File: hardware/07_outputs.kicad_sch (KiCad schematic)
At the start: 13 parts, among them J701 G-Switch GT-3321667P-01, J702 HRO PJ-332A-6A, J703 1 × 6

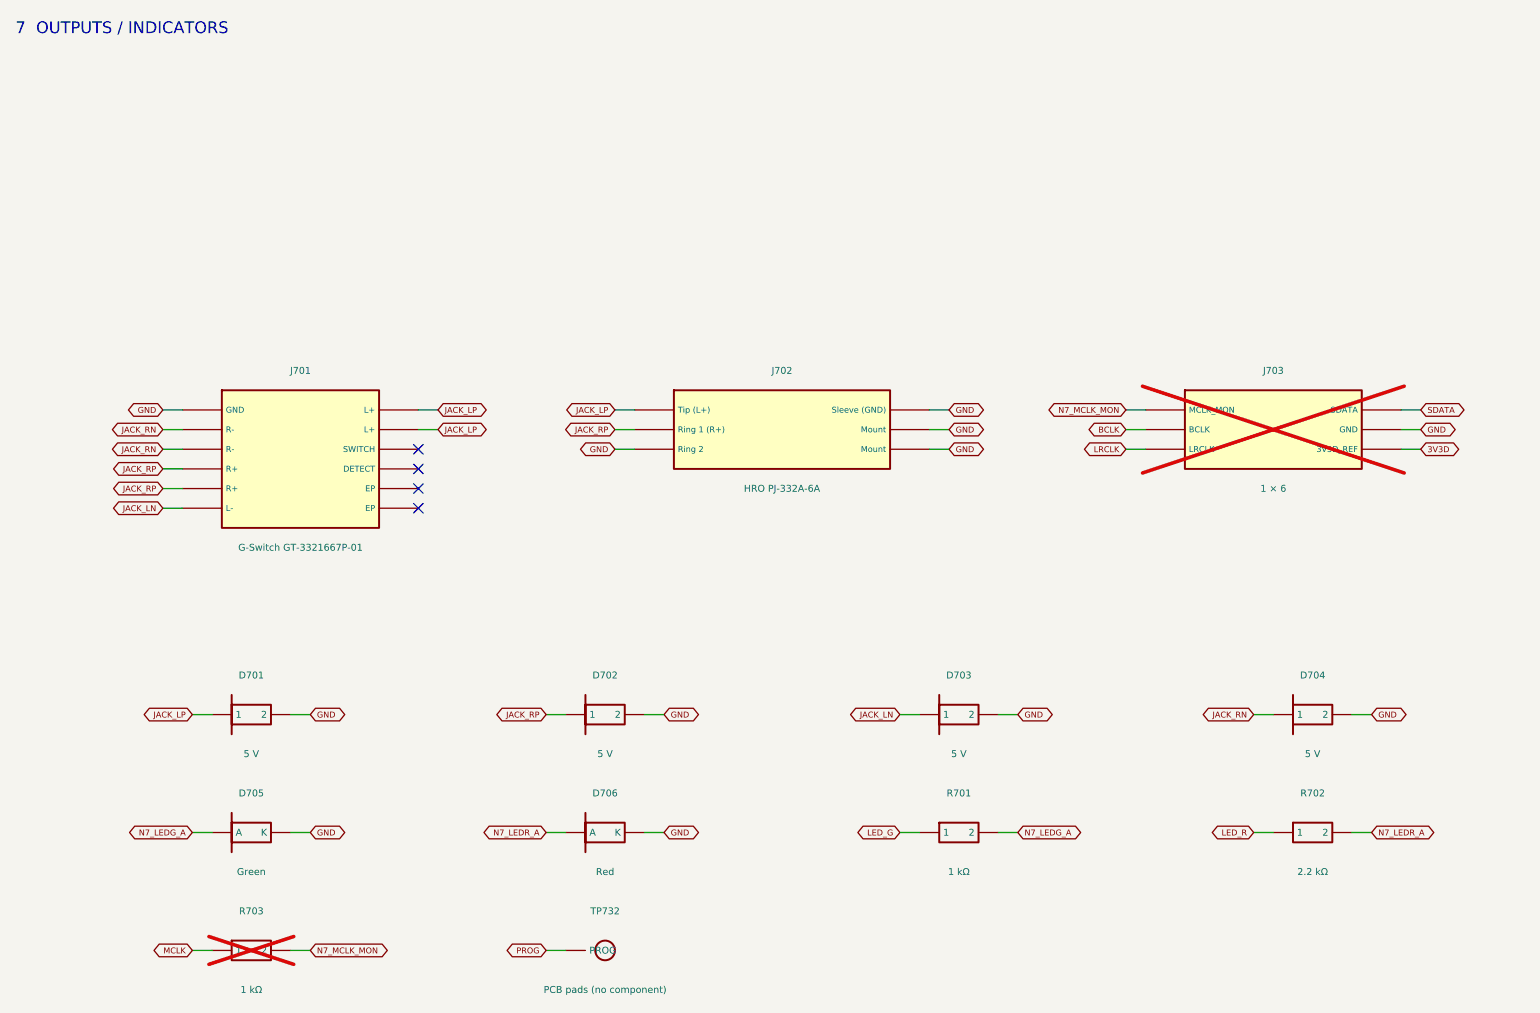
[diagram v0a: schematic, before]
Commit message: Recapture DAC-HPA schematic for design set v1.1
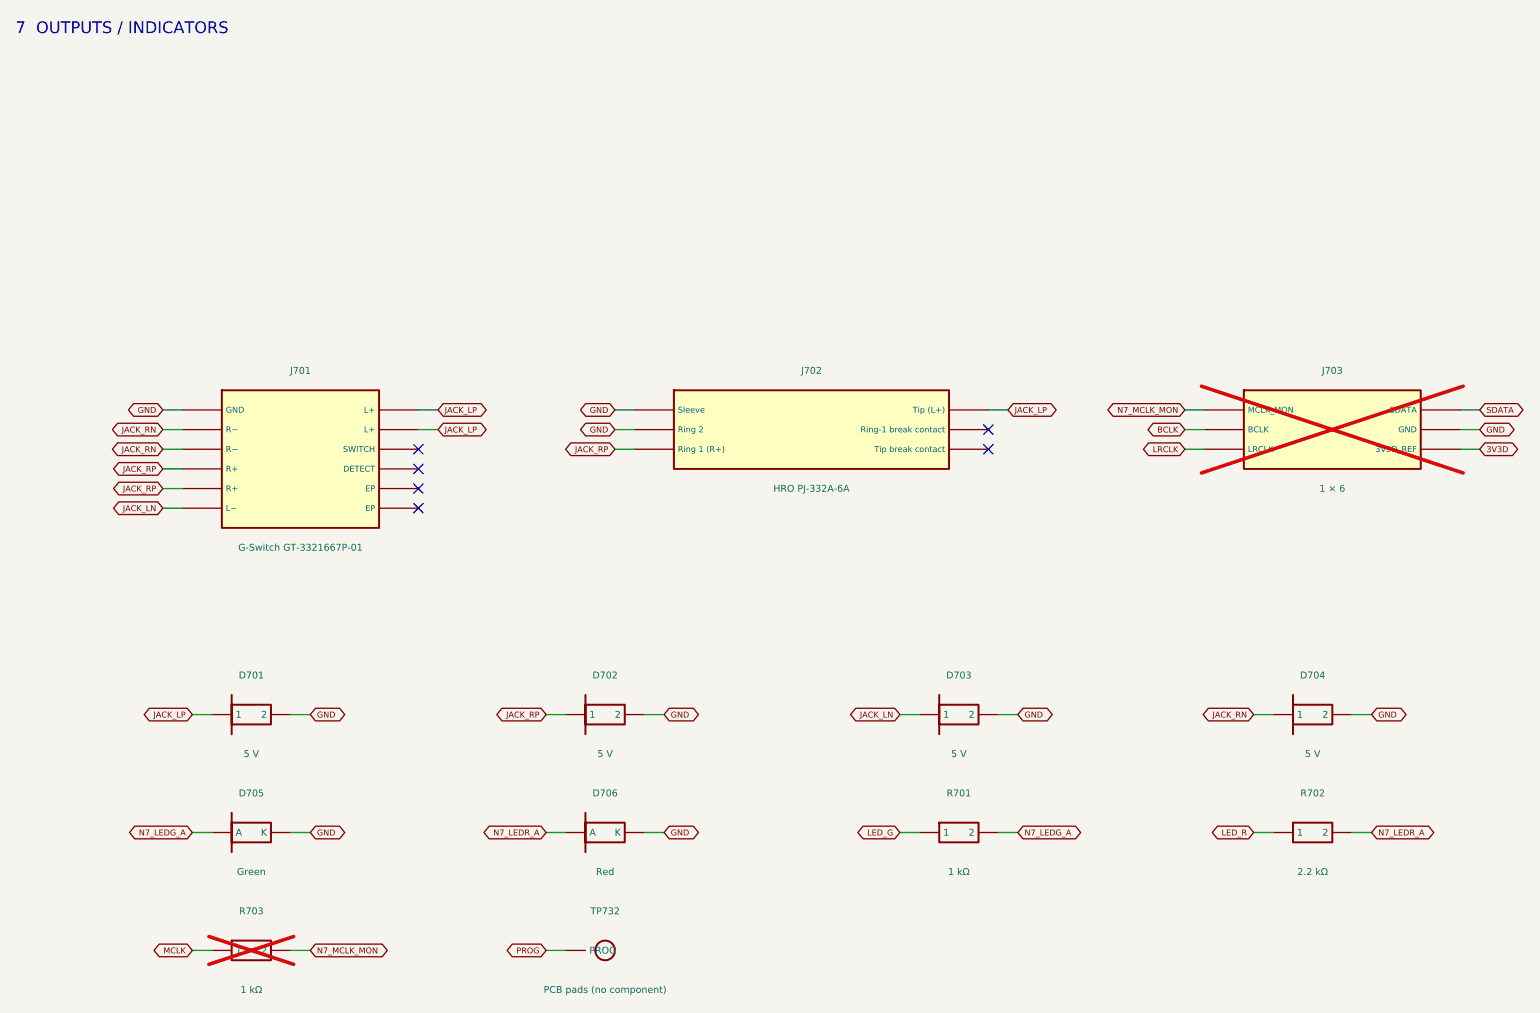
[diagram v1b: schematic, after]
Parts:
- D701, D702, D703, D704: symbol DAC_HPA:P170 -> DAC_HPA:P173
- D705: symbol DAC_HPA:P171 -> DAC_HPA:P174
- D706: symbol DAC_HPA:P172 -> DAC_HPA:P175
- J701: footprint JLC_Imported:AUDIO-TH_GT-3321667P-01 -> DAC_HPA:J701_GT-3321667P-01_maker_slots; symbol DAC_HPA:P173 -> DAC_HPA:P176
- J702: footprint JLC_Imported:AUDIO-SMD_PJ-332A-6A -> DAC_HPA:J702_PJ-332A-6A_peg_holes; symbol DAC_HPA:P174 -> DAC_HPA:P177; Package SMD -> SMD with two plated slot terminals
- J703: symbol DAC_HPA:P175 -> DAC_HPA:P178
- R701: symbol DAC_HPA:P176 -> DAC_HPA:P179
- R702: symbol DAC_HPA:P177 -> DAC_HPA:P180
- R703: symbol DAC_HPA:P178 -> DAC_HPA:P181
- TP732: symbol DAC_HPA:P179 -> DAC_HPA:P182
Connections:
- net GND: now also J702.1 (Sleeve), J702.2 (Ring 2); no longer J702.3 (Ring 2), J702.4 (Sleeve (GND)), J702.5 (Mount), J702.6 (Mount)
- net JACK_LP: now also J702.4 (Tip (L+)); no longer J702.1 (Tip (L+))
- net JACK_RP: now also J702.3 (Ring 1 (R+)); no longer J702.2 (Ring 1 (R+))
- no-connect marks 4 -> 6
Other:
- moved on the sheet: J702, J703

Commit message: Capture functional ECO and manual 120x100 review board
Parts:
- added D707, D708: 5 V, JLC_Imported:SOD-523_L1.2-W0.8-LS1.6-BI, symbol DAC_HPA:P9005
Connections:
- net GND: now also D707.2, D708.2
- net JACK_LP: now also D708.1
- net JACK_RP: now also D707.1
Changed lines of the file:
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@@
 (generator_version "10.0")
 (paper "A4")
-(title_block (title "7  OUTPUTS / INDICATORS") (date "2026-09-27") (rev "v1.1") (comment 1 "Design Spec v1.1 / Notes v1.0 / Parts List v0.9") (comment 2 "REVIEW ONLY: G-1 to G-4 remain open; J701/J702 maps from maker drawings"))
+(title_block (title "7  OUTPUTS / INDICATORS") (date "2026-09-28") (rev "v1.1-ECO1") (comment 1 "Spec v1.1 / Notes v1.0 / Parts List v0.9 + ECO F02/F04") (comment 2 "REVIEW ONLY: capture F01, attach F03 and G-1 to G-4 open"))
 (text "7  OUTPUTS / INDICATORS" (exclude_from_sim no) (at 20.32 15.24 0) (effects (font (size 1.524 1.524)) (justify left bottom)))
 (symbol (lib_id "DAC_HPA:P173") (at 50.8 102.87 0) (unit 1) (exclude_from_sim no) (in_bom yes) (on_board yes) (dnp no)
@@
 (wire (pts (xy 101.6 118.11) (xy 104.14 118.11)) (stroke (width 0) (type solid)))
 (global_label "GND" (shape bidirectional) (at 104.14 118.11 0) (effects (font (size 0.762 0.762)) (justify left bottom)))
+(symbol (lib_id "DAC_HPA:P9005") (at 142.24 133.35 0) (unit 1) (exclude_from_sim no) (in_bom yes) (on_board yes) (dnp no)
+(property "Reference" "D707" (at 142.24 128.27 0) (effects (font (size 0.889 0.889))))
+(property "Value" "5 V" (at 142.24 138.43 0) (effects (font (size 0.889 0.889))))
+(property "Footprint" "JLC_Imported:SOD-523_L1.2-W0.8-LS1.6-BI" (at 142.24 133.35 0) (effects (font (size 1.016 1.016)) (hide yes)))
+(property "Datasheet" "https://wmsc.lcsc.com/wmsc/upload/file/pdf/v2/lcsc/2412061650_GOODWORK-LESD5D5-0CT1G_C41399463.pdf" (at 142.24 133.35 0) (effects (font (size 1.016 1.016)) (hide yes)))
+(property "MPN" "GOODWORK LESD5D5.0CT1G" (at 142.24 133.35 0) (effects (font (size 1.016 1.016)) (hide yes)))
+(property "LCSC" "C41399463" (at 142.24 133.35 0) (effects (font (size 1.016 1.016)) (hide yes)))
+(property "LCSC Part #" "C41399463" (at 142.24 133.35 0) (effects (font (size 1.016 1.016)) (hide yes)))
+(property "Assembly" "Yes" (at 142.24 133.35 0) (effects (font (size 1.016 1.016)) (hide yes)))
+(property "Package" "SOD-523" (at 142.24 133.35 0) (effects (font (size 1.016 1.016)) (hide yes)))
+(property "Rating/Tolerance" "Bidirectional (datasheet V-I figure); VRWM 5 V, VBR 7 V (≥ 6 V min), VC ≤ 16 V at IPP 7 A 8/20 µs, CJ 12 pF typ, IR ≤ 1 µA at 5 V (datasheet listing); IEC 61000-4-2 level 4" (at 142.24 133.35 0) (effects (font (size 1.016 1.016)) (hide yes)))
+(property "Source" "JLCPCB library" (at 142.24 133.35 0) (effects (font (size 1.016 1.016)) (hide yes)))
+(property "Workbook Value" "— (functional ECO; absent from Parts List v0.9)" (at 142.24 133.35 0) (effects (font (size 1.016 1.016)) (hide yes)))
+(property "Footprint status" "VERIFY G-3" (at 142.24 133.35 0) (effects (font (size 1.016 1.016)) (hide yes)))
+(pin "1")
+(pin "2")
+(instances (project "DAC_HPA" (path "/0c6c0976-e401-5c8a-8977-bc60da031e5e/58a9838a-c006-5cfd-a571-921e8dbe4372" (reference "D707") (unit 1))))
+)
+(wire (pts (xy 137.16 133.35) (xy 134.62 133.35)) (stroke (width 0) (type solid)))
+(global_label "JACK_RP" (shape bidirectional) (at 134.62 133.35 180) (effects (font (size 0.762 0.762)) (justify right bottom)))
+(wire (pts (xy 147.32 133.35) (xy 149.86 133.35)) (stroke (width 0) (type solid)))
+(global_label "GND" (shape bidirectional) (at 149.86 133.35 0) (effects (font (size 0.762 0.762)) (justify left bottom)))
+(symbol (lib_id "DAC_HPA:P9005") (at 187.96 133.35 0) (unit 1) (exclude_from_sim no) (in_bom yes) (on_board yes) (dnp no)
+(property "Reference" "D708" (at 187.96 128.27 0) (effects (font (size 0.889 0.889))))
+(property "Value" "5 V" (at 187.96 138.43 0) (effects (font (size 0.889 0.889))))
+(property "Footprint" "JLC_Imported:SOD-523_L1.2-W0.8-LS1.6-BI" (at 187.96 133.35 0) (effects (font (size 1.016 1.016)) (hide yes)))
+(property "Datasheet" "https://wmsc.lcsc.com/wmsc/upload/file/pdf/v2/lcsc/2412061650_GOODWORK-LESD5D5-0CT1G_C41399463.pdf" (at 187.96 133.35 0) (effects (font (size 1.016 1.016)) (hide yes)))
+(property "MPN" "GOODWORK LESD5D5.0CT1G" (at 187.96 133.35 0) (effects (font (size 1.016 1.016)) (hide yes)))
+(property "LCSC" "C41399463" (at 187.96 133.35 0) (effects (font (size 1.016 1.016)) (hide yes)))
+(property "LCSC Part #" "C41399463" (at 187.96 133.35 0) (effects (font (size 1.016 1.016)) (hide yes)))
+(property "Assembly" "Yes" (at 187.96 133.35 0) (effects (font (size 1.016 1.016)) (hide yes)))
+(property "Package" "SOD-523" (at 187.96 133.35 0) (effects (font (size 1.016 1.016)) (hide yes)))
+(property "Rating/Tolerance" "Bidirectional (datasheet V-I figure); VRWM 5 V, VBR 7 V (≥ 6 V min), VC ≤ 16 V at IPP 7 A 8/20 µs, CJ 12 pF typ, IR ≤ 1 µA at 5 V (datasheet listing); IEC 61000-4-2 level 4" (at 187.96 133.35 0) (effects (font (size 1.016 1.016)) (hide yes)))
+(property "Source" "JLCPCB library" (at 187.96 133.35 0) (effects (font (size 1.016 1.016)) (hide yes)))
+(property "Workbook Value" "— (functional ECO; absent from Parts List v0.9)" (at 187.96 133.35 0) (effects (font (size 1.016 1.016)) (hide yes)))
+(property "Footprint status" "VERIFY G-3" (at 187.96 133.35 0) (effects (font (size 1.016 1.016)) (hide yes)))
+(pin "1")
+(pin "2")
+(instances (project "DAC_HPA" (path "/0c6c0976-e401-5c8a-8977-bc60da031e5e/58a9838a-c006-5cfd-a571-921e8dbe4372" (reference "D708") (unit 1))))
+)
+(wire (pts (xy 182.88 133.35) (xy 180.34 133.35)) (stroke (width 0) (type solid)))
+(global_label "JACK_LP" (shape bidirectional) (at 180.34 133.35 180) (effects (font (size 0.762 0.762)) (justify right bottom)))
+(wire (pts (xy 193.04 133.35) (xy 195.58 133.35)) (stroke (width 0) (type solid)))
+(global_label "GND" (shape bidirectional) (at 195.58 133.35 0) (effects (font (size 0.762 0.762)) (justify left bottom)))
 (symbol (lib_id "DAC_HPA:P176") (at 57.15 69.85 0) (unit 1) (exclude_from_sim no) (in_bom yes) (on_board yes) (dnp no)
 (property "Reference" "J701" (at 57.15 58.42 0) (effects (font (size 0.889 0.889))))
